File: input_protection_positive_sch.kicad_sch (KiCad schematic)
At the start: 23 parts, among them Q1 SQM110P06, Q2 MMBT3906, Q3 SQM110P06

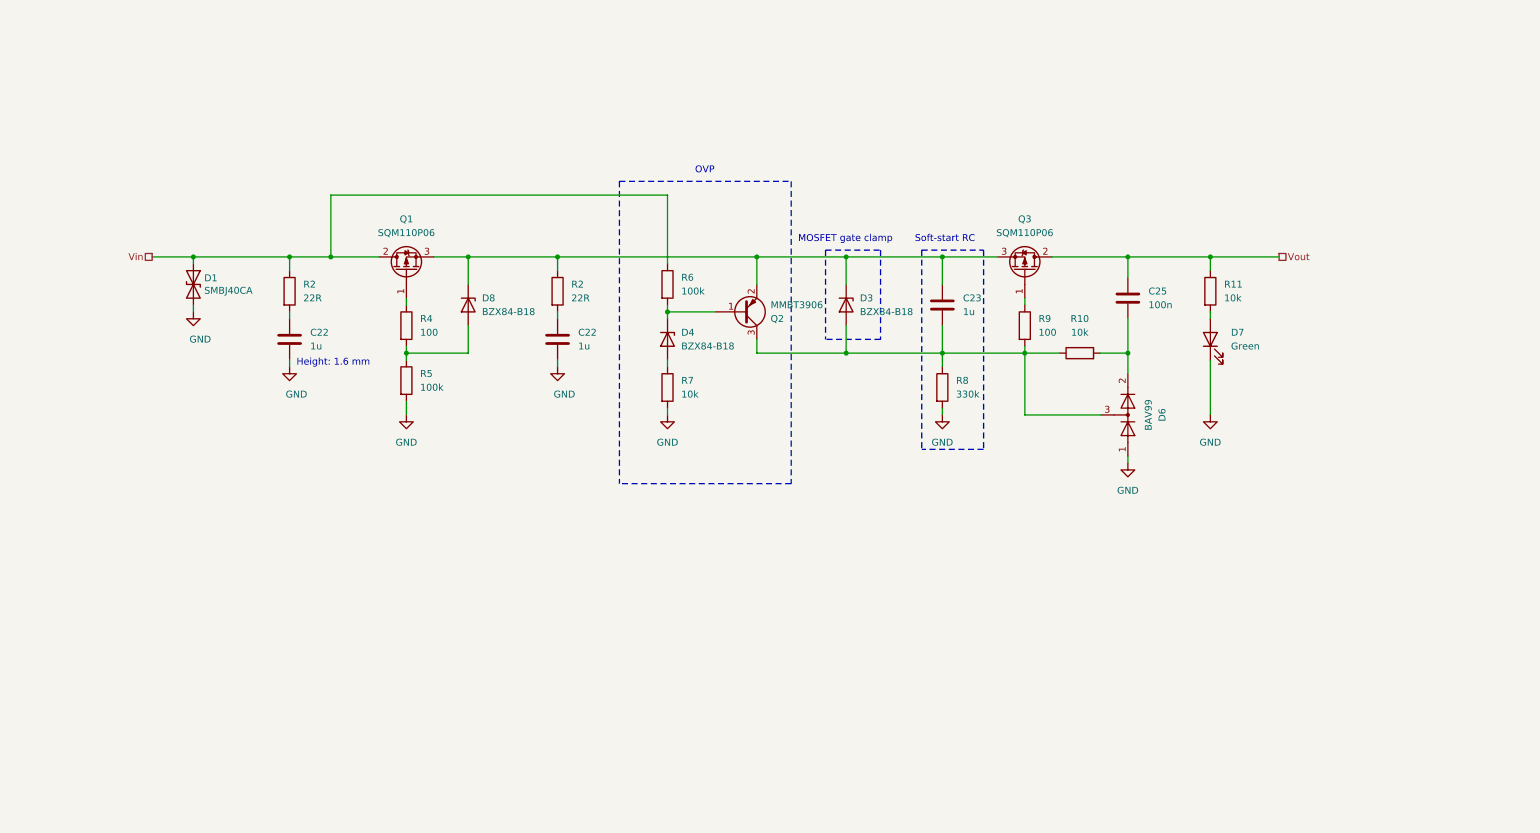
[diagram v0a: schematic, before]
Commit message: Added an input protection circuit Added CI
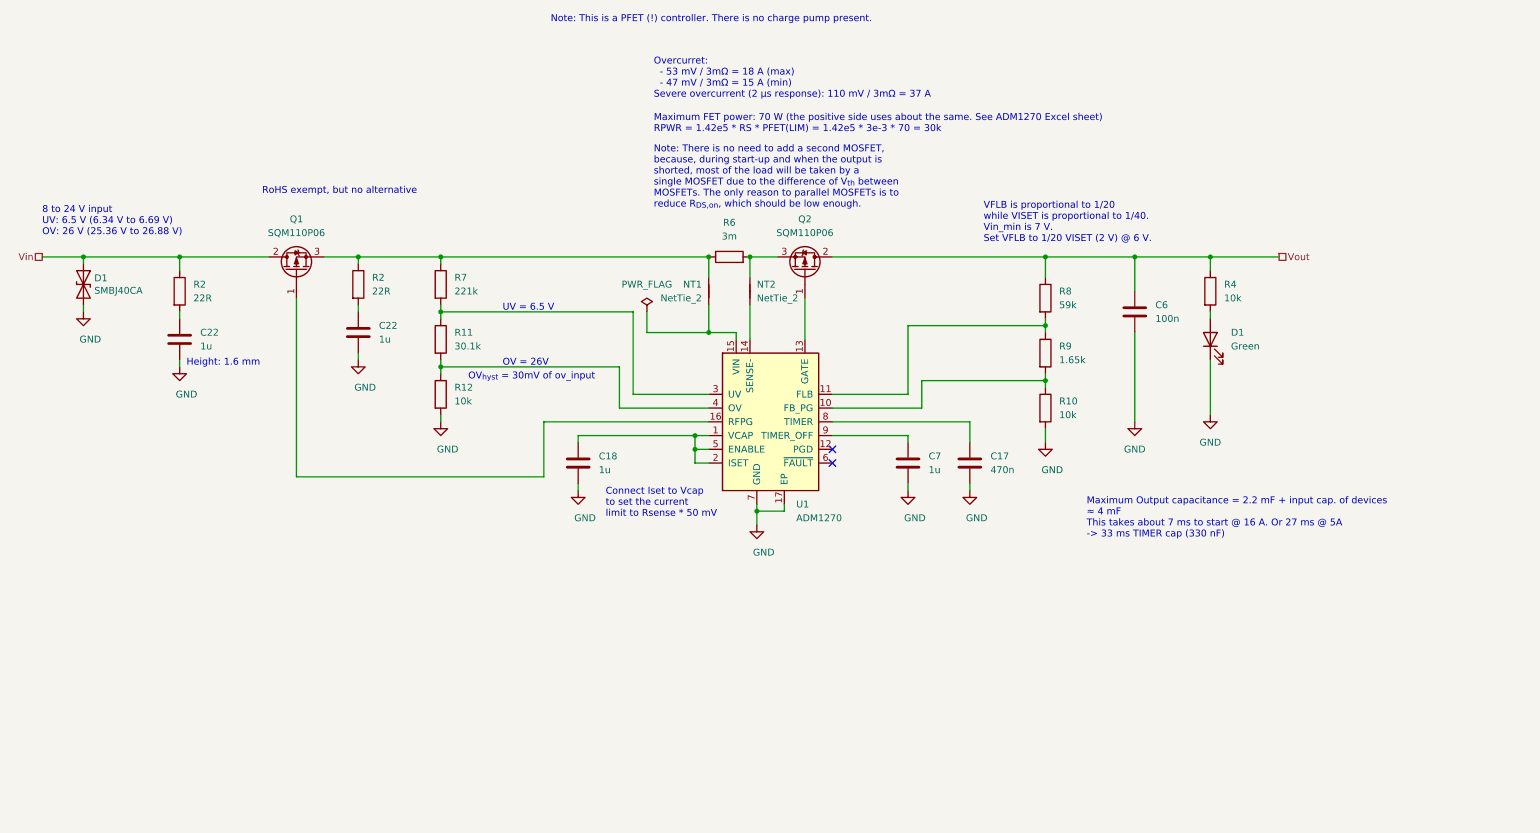
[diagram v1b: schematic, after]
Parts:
- removed C22 (x2), C23: 1u, Capacitor_SMD:C_1206_3216Metric, symbol Device:C
- removed C25: 100n, Capacitor_SMD:C_1206_3216Metric, symbol Device:C
- removed D3, D4, D8: BZX84-B18, Package_TO_SOT_SMD:SOT-23, symbol Diode:BZX84Cxx
- removed D6: BAV99, Package_TO_SOT_SMD:SOT-23, symbol Diode:BAV99
- removed D7: Green, LED_SMD:LED_0603_1608Metric, symbol Device:LED
- removed Q2: MMBT3906, Package_TO_SOT_SMD:SOT-23, symbol Transistor_BJT:MMBT3906
- removed Q3: SQM110P06, Package_TO_SOT_SMD:TO-263-2, symbol Device:Q_PMOS_GDS
- removed R2 (x2): 22R, Resistor_SMD:R_1206_3216Metric, symbol Device:R
- removed R5: 100k, Resistor_SMD:R_0805_2012Metric, symbol Device:R
- added C17: 470n, Capacitor_SMD:C_1206_3216Metric, symbol Device:C
- added C18, C22 (x2), C7: 1u, Capacitor_SMD:C_1206_3216Metric, symbol Device:C
- added C6: 100n, Capacitor_SMD:C_0805_2012Metric, symbol Device:C
- added D1: Green, LED_SMD:LED_0603_1608Metric, symbol Device:LED
- added NT1, NT2: NetTie_2, Custom_footprints:NET-TIE-0.20mm, symbol Device:NetTie_2
- added Q2: SQM110P06, Package_TO_SOT_SMD:TO-263-2, symbol Device:Q_PMOS_GDS
- added R12: 10k, Resistor_SMD:R_0805_2012Metric, symbol Device:R
- added R2 (x2): 22R, Resistor_SMD:R_1206_3216Metric, symbol Device:R
- added U1: ADM1270, Package_DFN_QFN:QFN-16-1EP_3x3mm_P0.5mm_EP1.45x1.45mm, symbol ADI:ADM1270ACPZ
- D1: MFN Bourns -> Littlefuse; PN SMBJ40CA-QH -> SZ1SMB40CAT3G; RoHS (none) -> Yes; Temperature (none) -> Tstorage = –55 °C to 150 °C
- Q1: Note (none) -> Vds >= 60V; RoHS (none) -> By exemption; Temperature (none) -> Tstorage = –75 °C to 175 °C
- R10: Note (none) -> 1%, 150 V; RoHS (none) -> By exemption; Temperature (none) -> Tstorage = –55 °C to 155 °C
- R11: value 10k -> 30.1k; Note (none) -> 1%, 150 V; PN CRCW080510K0FKEA -> CRCW080530K1FKEA; RoHS (none) -> By exemption; Temperature (none) -> Tstorage = –55 °C to 155 °C
- R4: value 100 -> 10k; Note (none) -> 1%, 150 V; PN CRCW0805100RFKEA -> CRCW080510K0FKEA; RoHS (none) -> By exemption; Temperature (none) -> Tstorage = –55 °C to 155 °C
- R6: value 100k -> 3m; footprint Resistor_SMD:R_0805_2012Metric -> Resistor_SMD:R_2512_6332Metric; MFN Vishay -> Bourns; PN CRCW0805100KFKEA -> CRE2512-FZ-R003E-3; RoHS (none) -> By exemption; Temperature (none) -> Tstorage = –75 °C to 170 °C
- R7: value 10k -> 221k; Note (none) -> 1%, 150 V; PN CRCW080510K0FKEA -> CRCW0805221KFKEA; RoHS (none) -> By exemption; Temperature (none) -> Tstorage = –55 °C to 155 °C
- R8: value 330k -> 59k; Note (none) -> 1%, 150 V; PN CRCW0805330KFKEA -> CRCW080559K0FKEA; RoHS (none) -> By exemption; Temperature (none) -> Tstorage = –55 °C to 155 °C
- R9: value 100 -> 1.65k; Note (none) -> 1%, 150 V; PN CRCW0805100RFKEA -> CRCW08051K65FKEA; RoHS (none) -> By exemption; Temperature (none) -> Tstorage = –55 °C to 155 °C
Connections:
- net GND: now also R10.2, C17.2, C18.2, C22.2, C22.2, C6.2, C7.2, D1.1 (K), R12.2, U1.17 (EP), U1.7 (GND); no longer R7.2, R8.2
- net Vin: now also R2.1; no longer R6.1
- net Vout: now also R4.1, R8.1, C6.1, Q2.2 (D); no longer R11.1
- net at R10.1, R9.2: now also U1.10 (FB_PG); no longer R8.1
- net at Q1.3 (S): now also R6.1, R7.1, NT1.2, R2.1
- net at R6.2: now also NT2.2, Q2.3 (S)
- net at R4.2: now also D1.2 (A)
- net at R9.1: now also R8.2, U1.11 (FLB)
- net at Q1.1 (G): now also U1.16 (RFPG); no longer R4.1
- net at R11.2: now also R12.1, U1.4 (OV)
- new net: R11.1, R7.2, U1.3 (UV)
- new net: C22.1, R2.2 (x2)
- new net: C7.1, U1.9 (TIMER_OFF)
- new net: C18.1, U1.1 (VCAP), U1.2 (ISET), U1.5 (ENABLE)
- new net: NT1.1, U1.15 (VIN)
- new net: NT2.1, U1.14 (SENSE-)
- new net: Q2.1 (G), U1.13 (GATE)
- new net: C17.1, U1.8 (TIMER)
- no-connect marks 0 -> 2
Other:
- note added: "8 to 24 V input UV: 6.5 V (6.34 V to 6.69 V) OV: 26 V (25.36 V to 26.88 V)"
- note added: "Connect Iset to Vcap to set the current limit to Rsense * 50 mV"
- note added: "Maximum FET power: 70 W (the positive side uses about the same. See ADM1270 Excel sheet) RPWR = 1.42e5 * RS * PFET(LIM) = 1.42e5 * 3e-3 * 70 = 30k"
- note added: "Maximum Output capacitance = 2.2 mF + input cap. of devices ≈ 4 mF This takes about 7 ms to start @ 16 A. Or 27 ms @ 5A -> 33 ms TIMER cap (330 nF)"
- note added: "Note: There is no need to add a second MOSFET, because, during start-up and when the output is shorted, most of the load will be taken by a single MOSFET due to the difference of V_{th} between MOSFETs. The only reason to parallel MOSFETs is to reduce R_{DS,on}, which should be low enough."
- note added: "Note: This is a PFET (!) controller. There is no charge pump present."
- note added: "OV = 26V"
- note added: "OV_{hyst} = 30mV of ov_input"
- note added: "Overcurret: - 53 mV / 3mΩ = 18 A (max) - 47 mV / 3mΩ = 15 A (min) Severe overcurrent (2 µs response): 110 mV / 3mΩ = 37 A"
- note added: "RoHS exempt, but no alternative"
- note added: "UV = 6.5 V"
- note added: "VFLB is proportional to 1/20 while VISET is proportional to 1/40. Vin_min is 7 V. Set VFLB to 1/20 VISET (2 V) @ 6 V."
- note removed: "MOSFET gate clamp"
- note removed: "OVP"
- note removed: "Soft-start RC"
- title: (none) -> Positive rail input protection
- moved on the sheet: Q1

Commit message: Added Ferrite beads at the board input Moved power connector silkscreen labels Added TODO list for v.2.1.0
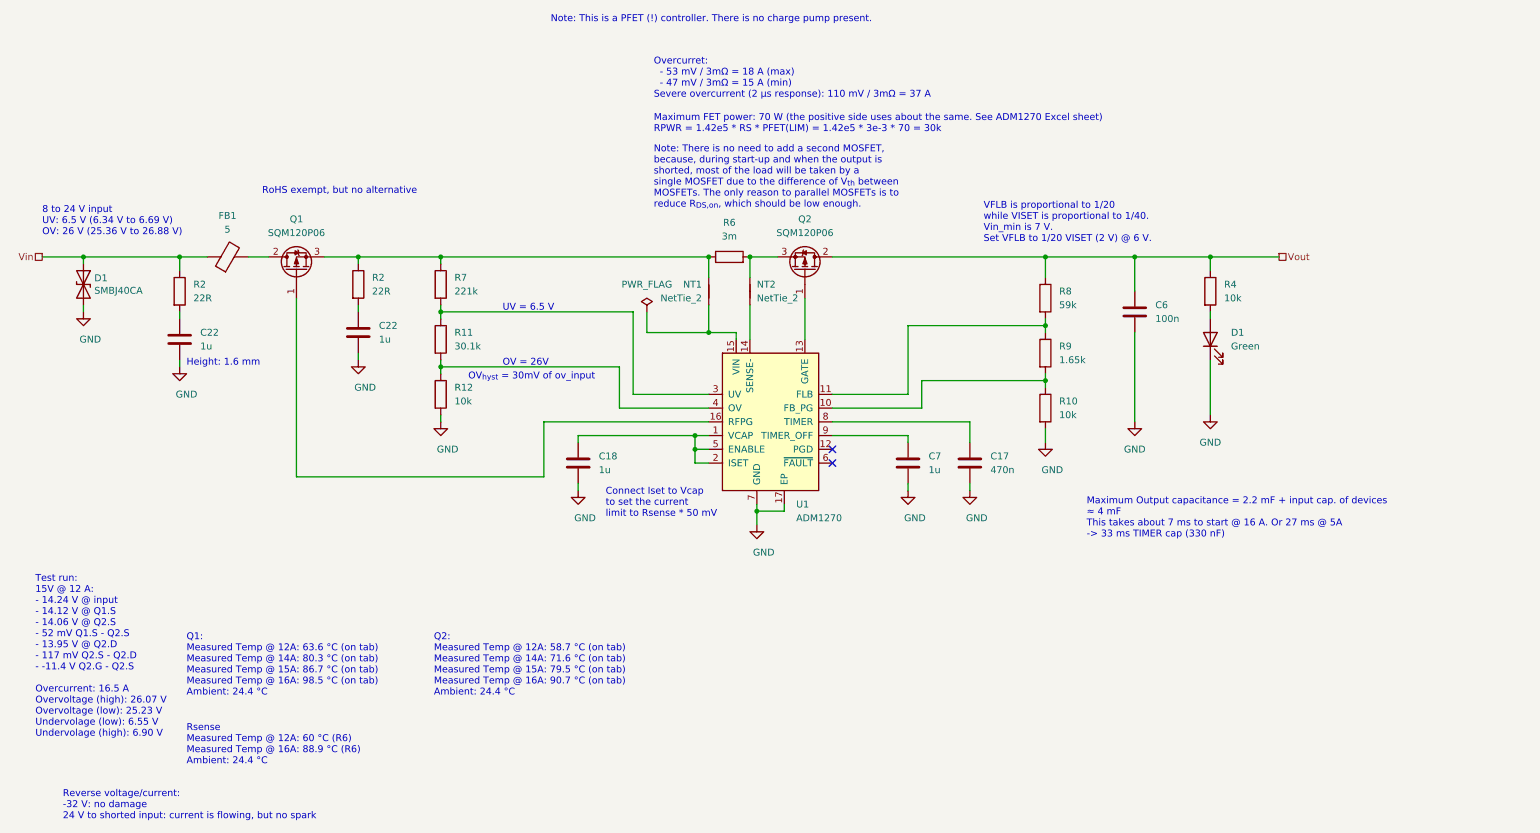
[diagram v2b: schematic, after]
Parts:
- added FB1: 5, Inductor_SMD:L_1210_3225Metric, symbol Device:FerriteBead
- Q1, Q2: value SQM110P06 -> SQM120P06; PN SQM110P06-8m9L -> SQM120P06-07L
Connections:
- net Vin: now also FB1.1; no longer Q1.2 (D)
- new net: FB1.2, Q1.2 (D)
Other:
- note added: "Q1: Measured Temp @ 12A: 63.6 °C (on tab) Measured Temp @ 14A: 80.3 °C (on tab) Measured Temp @ 15A: 86.7 °C (on tab) Measured Temp @ 16A: 98.5 °C (on tab) Ambient: 24.4 °C"
- note added: "Q2: Measured Temp @ 12A: 58.7 °C (on tab) Measured Temp @ 14A: 71.6 °C (on tab) Measured Temp @ 15A: 79.5 °C (on tab) Measured Temp @ 16A: 90.7 °C (on tab) Ambient: 24.4 °C"
- note added: "Reverse voltage/current: -32 V: no damage 24 V to shorted input: current is flowing, but no spark"
- note added: "Rsense Measured Temp @ 12A: 60 °C (R6) Measured Temp @ 16A: 88.9 °C (R6) Ambient: 24.4 °C"
- note added: "Test run: 15V @ 12 A: - 14.24 V @ input - 14.12 V @ Q1.S - 14.06 V @ Q2.S - 52 mV Q1.S - Q2.S - 13.95 V @ Q2.D - 117 mV Q2.S - Q2.D - -11.4 V Q2.G - Q2.S Overcurrent: 16.5 A Overvoltage (high): 26.07 V Overvoltage (low): 25.23 V Undervolage (low): 6.55 V Undervolage (high): 6.90 V"
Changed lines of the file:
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@@
+    (stroke (width 0) (type default))
+  )
+  (wire (pts (xy 58.42 64.77) (xy 62.23 64.77))
     (stroke (width 0) (type default))
   )
@@
     (stroke (width 0) (type default))
   )
-  (wire (pts (xy 45.72 64.77) (xy 62.23 64.77))
-    (stroke (width 0) (type default))
-  )
   (wire (pts (xy 45.72 64.77) (xy 45.72 67.31))
     (stroke (width 0) (type default))
@@
     (stroke (width 0) (type default))
   )
+  (wire (pts (xy 45.72 64.77) (xy 50.8 64.77))
+    (stroke (width 0) (type default))
+  )
   (wire (pts (xy 78.74 82.55) (xy 78.74 83.82))
     (stroke (width 0) (type default))
@@
   (wire (pts (xy 151.13 64.77) (xy 156.21 64.77))
     (stroke (width 0) (type default))
+  )
+  (text "\nQ2:\nMeasured Temp @ 12A: 58.7 °C (on tab)\nMeasured Temp @ 14A: 71.6 °C (on tab)\nMeasured Temp @ 15A: 79.5 °C (on tab)\nMeasured Temp @ 16A: 90.7 °C (on tab)\nAmbient: 24.4 °C"
+    (at 92.71 146.05 0)
+    (effects (font (size 1.27 1.27)) (justify left bottom))
   )
   (text "OV = 26V" (at 105.41 85.09 0)
@@
     (effects (font (size 1.27 1.27)) (justify left bottom))
   )
+  (text "Q1:\nMeasured Temp @ 12A: 63.6 °C (on tab)\nMeasured Temp @ 14A: 80.3 °C (on tab)\nMeasured Temp @ 15A: 86.7 °C (on tab)\nMeasured Temp @ 16A: 98.5 °C (on tab)\nAmbient: 24.4 °C"
+    (at 46.99 146.05 0)
+    (effects (font (size 1.27 1.27)) (justify left bottom))
+  )
   (text "RoHS exempt, but no alternative" (at 60.96 53.34 0)
     (effects (font (size 1.27 1.27)) (justify left bottom))
@@
     (effects (font (size 1.27 1.27)) (justify left bottom))
   )
+  (text "Rsense\nMeasured Temp @ 12A: 60 °C (R6)\nMeasured Temp @ 16A: 88.9 °C (R6)\nAmbient: 24.4 °C"
+    (at 46.99 158.75 0)
+    (effects (font (size 1.27 1.27)) (justify left bottom))
+  )
   (text "Note: This is a PFET (!) controller. There is no charge pump present."
     (at 114.3 21.59 0)
     (effects (font (size 1.27 1.27)) (justify left bottom))
   )
+  (text "Test run:\n15V @ 12 A:\n- 14.24 V @ input\n- 14.12 V @ Q1.S\n- 14.06 V @ Q2.S\n- 52 mV Q1.S - Q2.S\n- 13.95 V @ Q2.D\n- 117 mV Q2.S - Q2.D\n- -11.4 V Q2.G - Q2.S\n\nOvercurrent: 16.5 A\nOvervoltage (high): 26.07 V\nOvervoltage (low): 25.23 V\nUndervolage (low): 6.55 V\nUndervolage (high): 6.90 V"
+    (at 19.05 153.67 0)
+    (effects (font (size 1.27 1.27)) (justify left bottom))
+  )
   (text "Connect Iset to Vcap\nto set the current\nlimit to Rsense * 50 mV"
     (at 124.46 113.03 0)
@@
   (text "Overcurret:\n  - 53 mV / 3mΩ = 18 A (max)\n  - 47 mV / 3mΩ = 15 A (min)\nSevere overcurrent (2 µs response): 110 mV / 3mΩ = 37 A"
     (at 133.35 35.56 0)
+    (effects (font (size 1.27 1.27)) (justify left bottom))
+  )
+  (text "Reverse voltage/current:\n-32 V: no damage\n24 V to shorted input: current is flowing, but no spark"
+    (at 24.13 168.91 0)
     (effects (font (size 1.27 1.27)) (justify left bottom))
   )
@@
     )
   )
+  (symbol (lib_id "Device:FerriteBead") (at 54.61 64.77 90) (unit 1)
+    (in_bom yes) (on_board yes) (dnp no) (fields_autoplaced)
+    (property "Reference" "FB1" (at 54.5592 57.15 90)
+      (effects (font (size 1.27 1.27)))
+    )
+    (property "Value" "5" (at 54.5592 59.69 90)
+      (effects (font (size 1.27 1.27)))
+    )
+    (property "Footprint" "Inductor_SMD:L_1210_3225Metric" (at 54.61 66.548 90)
+      (effects (font (size 1.27 1.27)) hide)
+    )
+    (property "Datasheet" "~" (at 54.61 64.77 0)
+      (effects (font (size 1.27 1.27)) hide)
+    )
+    (property "MFN" "Murata" (at 54.61 64.77 0)
+      (effects (font (size 1.27 1.27)) hide)
+    )
+    (property "PN" "BLE32SN120BH1L" (at 54.61 64.77 0)
+      (effects (font (size 1.27 1.27)) hide)
+    )
+    (property "Alternative" "Murata BLE32SN120SH1L" (at 54.61 64.77 90)
+      (effects (font (size 1.27 1.27)) hide)
+    )
+    (property "Note" "" (at 54.61 64.77 90)
+      (effects (font (size 1.27 1.27)) hide)
+    )
+    (property "Temperature" "Tstorage = –55 °C to 150 °C" (at 54.61 64.77 0)
+      (effects (font (size 1.27 1.27)) hide)
+    )
+    (property "RoHS" "Yes" (at 54.61 64.77 0)
+      (effects (font (size 1.27 1.27)) hide)
+    )
+    (pin "1")
+    (pin "2")
+    (instances
+      (project "main"
+        (path "/b4ace06a-3ad4-479e-aaa4-d547ecf6903f/1acfc0a8-4adc-455e-9f2b-420811df0901"
+          (reference "FB1") (unit 1)
+        )
+        (path "/b4ace06a-3ad4-479e-aaa4-d547ecf6903f/f9160387-088e-4a7b-8d58-b2647e07444c"
+          (reference "FB2") (unit 1)
+        )
+      )
+    )
+  )
   (symbol (lib_id "power:GND") (at 236.22 93.98 0) (unit 1)
     (in_bom yes) (on_board yes) (dnp no) (fields_autoplaced)
@@
       (effects (font (size 1.27 1.27)))
     )
-    (property "Value" "SQM110P06" (at 67.31 60.325 90)
+    (property "Value" "SQM120P06" (at 67.31 60.325 90)
       (effects (font (size 1.27 1.27)))
     )
@@
       (effects (font (size 1.27 1.27)) hide)
     )
-    (property "PN" "SQM110P06-8m9L" (at 67.31 67.31 0)
+    (property "PN" "SQM120P06-07L" (at 67.31 67.31 0)
       (effects (font (size 1.27 1.27)) hide)
     )
@@
       (effects (font (size 1.27 1.27)))
     )
-    (property "Value" "SQM110P06" (at 161.29 60.325 90)
+    (property "Value" "SQM120P06" (at 161.29 60.325 90)
       (effects (font (size 1.27 1.27)))
     )
@@
       (effects (font (size 1.27 1.27)) hide)
     )
-    (property "PN" "SQM110P06-8m9L" (at 161.29 67.31 0)
-      (effects (font (size 1.27 1.27)) hide)
-    )
+    (property "PN" "SQM120P06-07L" (at 161.29 67.31 0)
+      (effects (font (size 1.27 1.27)) hide)
+    )
